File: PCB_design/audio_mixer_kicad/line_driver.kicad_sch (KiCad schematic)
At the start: 13 parts, among them U20 1606Q16-U

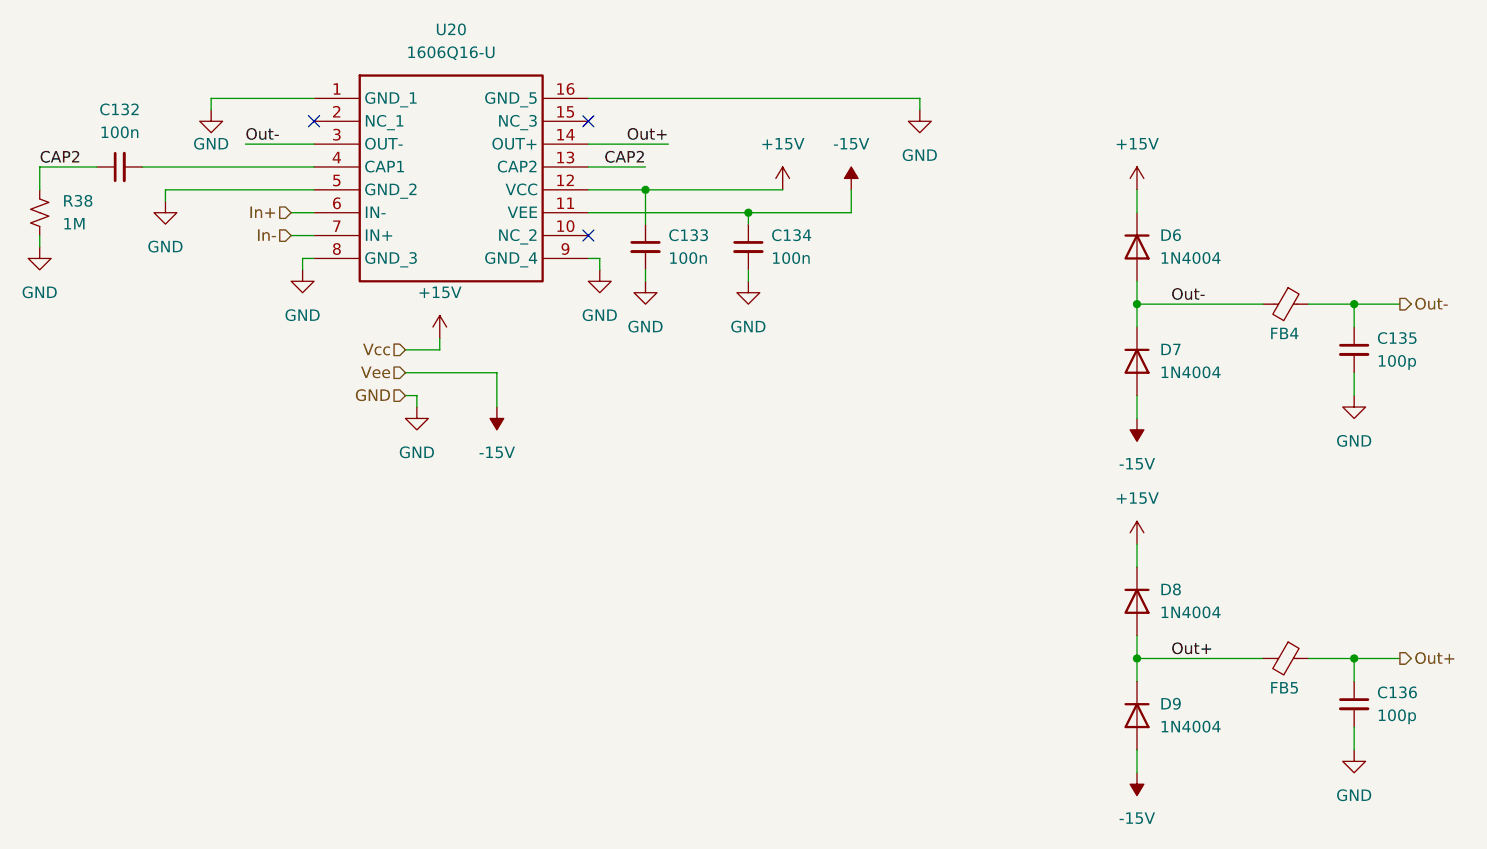
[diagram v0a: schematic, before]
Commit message: Reannotate and add passives for Y1
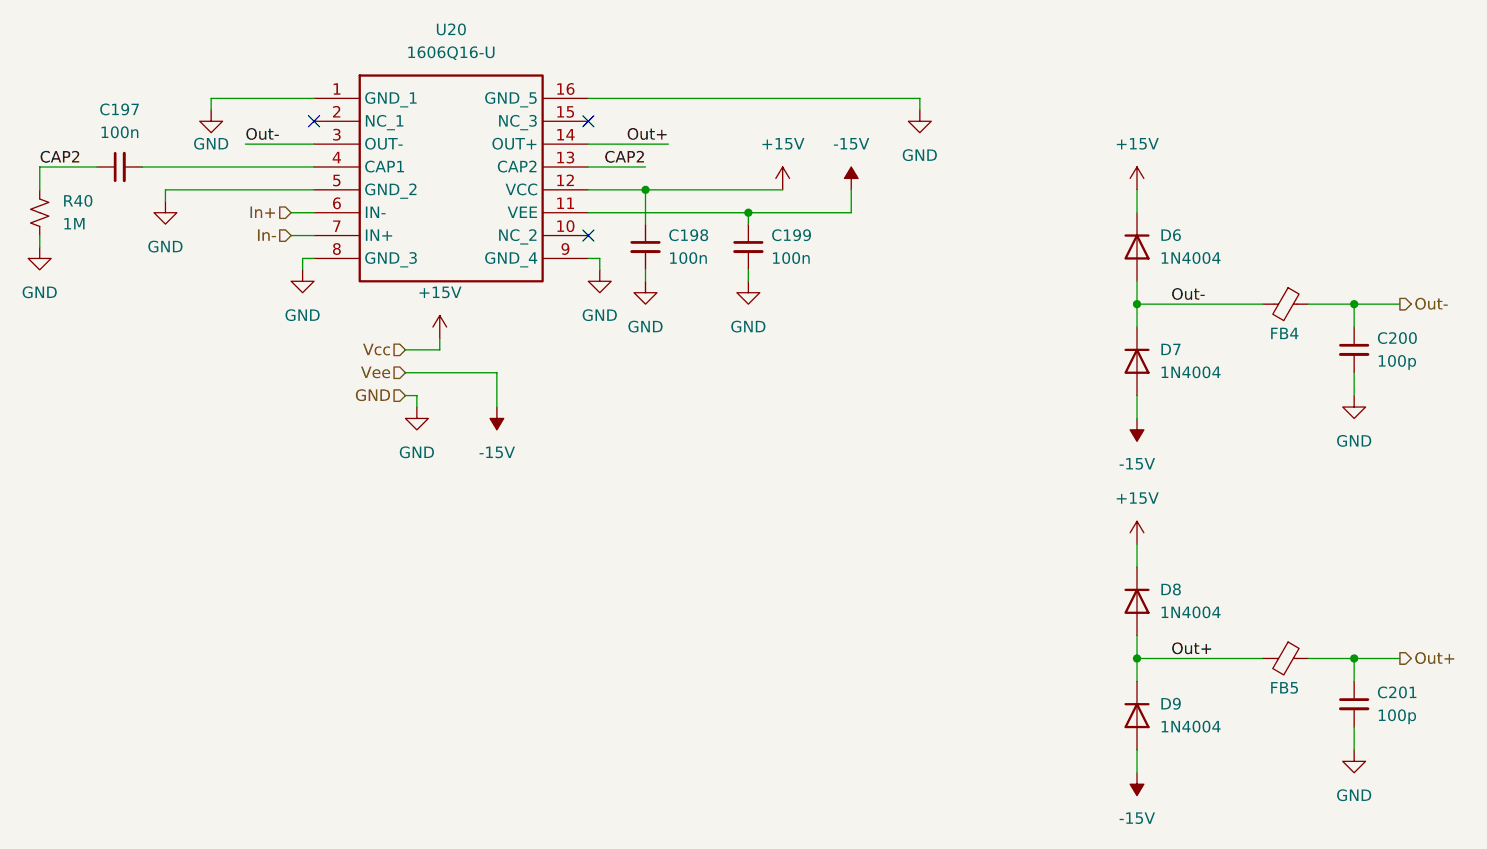
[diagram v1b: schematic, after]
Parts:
- renumbered C132 to C197, C133 to C198, C134 to C199, C135 to C200, C136 to C201, R38 to R40
